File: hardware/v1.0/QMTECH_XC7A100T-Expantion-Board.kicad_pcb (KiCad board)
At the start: 4 copper layers, 99.1 x 98.5 mm, 132 parts, among them J1 Micro_SD_Card_Det1, J10 Conn_01x06, J11 Conn_01x04, J12 Conn_01x34, J13 Conn_02x10_Odd_Even, J14 USB_C_Receptacle_USB2.0_16P, J15 Conn_02x06_Top_Bottom, J16 Conn_02x06_Top_Bottom, J2 Conn_01x34, J3 USB_C_Receptacle_USB2.0_16P, J4 Conn_01x34, J5 Conn_01x03, J6 Conn_01x03, J7 Conn_01x04, J8 Conn_01x34, J9 Conn_01x34, Q1 AON6411, U10 74LVC245A, U11 TLV62585, U12 CH32V003JxMx, U13 TLV75718PDRV, U14 HUSB238, U15 CH340C, U2 CH32V003JxMx, U4 ADV7180BCP32Z-RL, U5 TLV62585, U6 74LVC245A, U7 TLV62585, U8 74LVC245A, U9 74LVC245A, Y1 28.63636MHz

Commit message: first schematic iteration done
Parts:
- added REF**: LED_0805_2012Metric, LED_SMD:LED_0805_2012Metric, F.Cu at (158.0, 103.4)
- added REF**: LED_0805_2012Metric, LED_SMD:LED_0805_2012Metric, F.Cu at (158.0, 105.4)
- added REF**: LED_0805_2012Metric, LED_SMD:LED_0805_2012Metric, F.Cu at (158.0, 107.4)
- added REF**: LED_0805_2012Metric, LED_SMD:LED_0805_2012Metric, F.Cu at (154.4, 103.4)
- added REF**: LED_0805_2012Metric, LED_SMD:LED_0805_2012Metric, F.Cu at (154.4, 107.5)
- added REF**: LED_0805_2012Metric, LED_SMD:LED_0805_2012Metric, F.Cu at (158.0, 101.3)
- added REF**: LED_0805_2012Metric, LED_SMD:LED_0805_2012Metric, F.Cu at (154.4, 105.4)
- added REF**: LED_0805_2012Metric, LED_SMD:LED_0805_2012Metric, F.Cu at (154.4, 101.3)
- added U16: ~, Package_DFN_QFN:Diodes_UDFN-10_1.0x2.5mm_P0.5mm, F.Cu at (39.5, 90.2)
- added U3: ~, Package_DFN_QFN:Diodes_UDFN-10_1.0x2.5mm_P0.5mm, F.Cu at (36.3, 90.2)
- J15, J16: value Conn_02x06_Top_Bottom -> Conn_02x06_Odd_Even
- moved J15 22.9 mm to (68.1, 92.9)
- moved J16 22.9 mm to (68.1, 70.0)
- moved U15 18.8 mm to (30.3, 94.0)
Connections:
- J14 pad A1: Net-(J14-GND-PadA1) -> GND
- J14 pad A12: Net-(J14-GND-PadA1) -> GND
- J14 pad A4: Net-(J14-VBUS-PadA4) -> unconnected-(J14-VBUS-PadA4)
- J14 pad A5: unconnected-(J14-CC1-PadA5) -> Net-(J14-CC1)
- J14 pad A6: unconnected-(J14-D+-PadA6) -> /UART_DP
- J14 pad A7: unconnected-(J14-D--PadA7) -> /UART_DN
- J14 pad A9: Net-(J14-VBUS-PadA4) -> unconnected-(J14-VBUS-PadA4)_2
- J14 pad B1: Net-(J14-GND-PadA1) -> GND
- J14 pad B12: Net-(J14-GND-PadA1) -> GND
- J14 pad B4: Net-(J14-VBUS-PadA4) -> unconnected-(J14-VBUS-PadA4)_1
- J14 pad B5: unconnected-(J14-CC2-PadB5) -> Net-(J14-CC2)
- J14 pad B6: unconnected-(J14-D+-PadB6) -> /UART_DP
- J14 pad B7: unconnected-(J14-D--PadB7) -> /UART_DN
- J14 pad B9: Net-(J14-VBUS-PadA4) -> unconnected-(J14-VBUS-PadA4)_3
- J14 pad S1: unconnected-(J14-SHIELD-PadS1) -> Net-(J14-SHIELD)
- J15 pad 1: unconnected-(J15-Pin_1-Pad1) -> /PMOD0_0P
- J15 pad 10: unconnected-(J15-Pin_10-Pad10) -> GND
- J15 pad 11: unconnected-(J15-Pin_11-Pad11) -> +3V3
- J15 pad 12: unconnected-(J15-Pin_12-Pad12) -> +3V3
- J15 pad 2: unconnected-(J15-Pin_2-Pad2) -> /PMOD0_0N
- J15 pad 3: unconnected-(J15-Pin_3-Pad3) -> /PMOD0_1P
- J15 pad 4: unconnected-(J15-Pin_4-Pad4) -> /PMOD0_1N
- J15 pad 5: unconnected-(J15-Pin_5-Pad5) -> /PMOD0_2P
- J15 pad 6: unconnected-(J15-Pin_6-Pad6) -> /PMOD0_2N
- J15 pad 7: unconnected-(J15-Pin_7-Pad7) -> /PMOD0_3P
- J15 pad 8: unconnected-(J15-Pin_8-Pad8) -> /PMOD0_3N
- J15 pad 9: unconnected-(J15-Pin_9-Pad9) -> GND
- J16 pad 1: unconnected-(J16-Pin_1-Pad1) -> /PMOD1_0P
- J16 pad 10: unconnected-(J16-Pin_10-Pad10) -> GND
- J16 pad 11: unconnected-(J16-Pin_11-Pad11) -> +3V3
- J16 pad 12: unconnected-(J16-Pin_12-Pad12) -> +3V3
- J16 pad 2: unconnected-(J16-Pin_2-Pad2) -> /PMOD1_0N
- J16 pad 3: unconnected-(J16-Pin_3-Pad3) -> /PMOD1_1P
- J16 pad 4: unconnected-(J16-Pin_4-Pad4) -> /PMOD1_1N
- J16 pad 5: unconnected-(J16-Pin_5-Pad5) -> /PMOD1_2P
- J16 pad 6: unconnected-(J16-Pin_6-Pad6) -> /PMOD1_2N
- J16 pad 7: unconnected-(J16-Pin_7-Pad7) -> /PMOD1_3P
- J16 pad 8: unconnected-(J16-Pin_8-Pad8) -> /PMOD1_3N
- J16 pad 9: unconnected-(J16-Pin_9-Pad9) -> GND
- J3 pad S1: GND -> Net-(J3-SHIELD)
- U1 pad 71: unconnected-(U1B-IO_B5-Pad71) -> /PMOD1_3P
- U1 pad 72: unconnected-(U1B-IO_A5-Pad72) -> /PMOD1_3N
- U1 pad 73: unconnected-(U1B-IO_B4-Pad73) -> /PMOD1_2P
- U1 pad 74: unconnected-(U1B-IO_A4-Pad74) -> /PMOD1_2N
- U1 pad 75: unconnected-(U1B-IO_A3-Pad75) -> /PMOD1_1P
- U1 pad 76: unconnected-(U1B-IO_A2-Pad76) -> /PMOD1_1N
- U1 pad 77: unconnected-(U1B-IO_D4-Pad77) -> /PMOD1_0P
- U1 pad 78: unconnected-(U1B-IO_C4-Pad78) -> /PMOD1_0N
- U1 pad 79: unconnected-(U1B-IO_C2-Pad79) -> /PMOD0_3P
- U1 pad 80: unconnected-(U1B-IO_B2_VREF-Pad80) -> /PMOD0_3N
- U1 pad 81: unconnected-(U1B-IO_E5-Pad81) -> /PMOD0_2P
- U1 pad 82: unconnected-(U1B-IO_D5-Pad82) -> /PMOD0_2N
- U1 pad 83: unconnected-(U1B-IO_C1-Pad83) -> /PMOD0_1P
- U1 pad 84: unconnected-(U1B-IO_B1-Pad84) -> /PMOD0_1N
- U1 pad 85: unconnected-(U1B-IO_E1-Pad85) -> /PMOD0_0P
- U1 pad 86: unconnected-(U1B-IO_D1-Pad86) -> /PMOD0_0N
- U15 pad 1: unconnected-(U15-GND-Pad1) -> GND
- U15 pad 16: unconnected-(U15-VCC-Pad16) -> +3V3
- U15 pad 2: unconnected-(U15-TXD-Pad2) -> /UART_TX
- U15 pad 3: unconnected-(U15-RXD-Pad3) -> /UART_RX
- U15 pad 4: unconnected-(U15-V3-Pad4) -> +3V3
- U15 pad 5: unconnected-(U15-UD+-Pad5) -> /UART_DP
- U15 pad 6: unconnected-(U15-UD--Pad6) -> /UART_DN
- U15 pad 7: unconnected-(U15-NC-Pad7) -> (no net)
- U15 pad 8: unconnected-(U15-NC-Pad8) -> (no net)
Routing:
- net unconnected-(J15-Pin_6-Pad6): track 46.9 -> 0.00 mm
- net unconnected-(J15-Pin_8-Pad8): track 46.5 -> 0.00 mm
- net unconnected-(J15-Pin_7-Pad7): track 45.9 -> 0.00 mm
- net unconnected-(J15-Pin_5-Pad5): track 45.7 -> 0.00 mm
- net unconnected-(J15-Pin_11-Pad11): track 42.7 -> 0.00 mm
- net unconnected-(J15-Pin_9-Pad9): track 41.6 -> 0.00 mm
- net unconnected-(J15-Pin_10-Pad10): track 39.7 -> 0.00 mm
- net unconnected-(J15-Pin_12-Pad12): track 39.5 -> 0.00 mm
- net unconnected-(J16-Pin_12-Pad12): track 22.5 -> 0.00 mm
- net unconnected-(J16-Pin_10-Pad10): track 22.5 -> 0.00 mm
- net unconnected-(J16-Pin_11-Pad11): track 21.2 -> 0.00 mm
- net unconnected-(J16-Pin_9-Pad9): track 20.9 -> 0.00 mm
- net unconnected-(J16-Pin_7-Pad7): track 18.7 -> 0.00 mm
- net unconnected-(J16-Pin_5-Pad5): track 17.4 -> 0.00 mm
- net unconnected-(J16-Pin_8-Pad8): track 16.8 -> 0.00 mm
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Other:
- board text added: "USART"
- board text added: "USB PD"

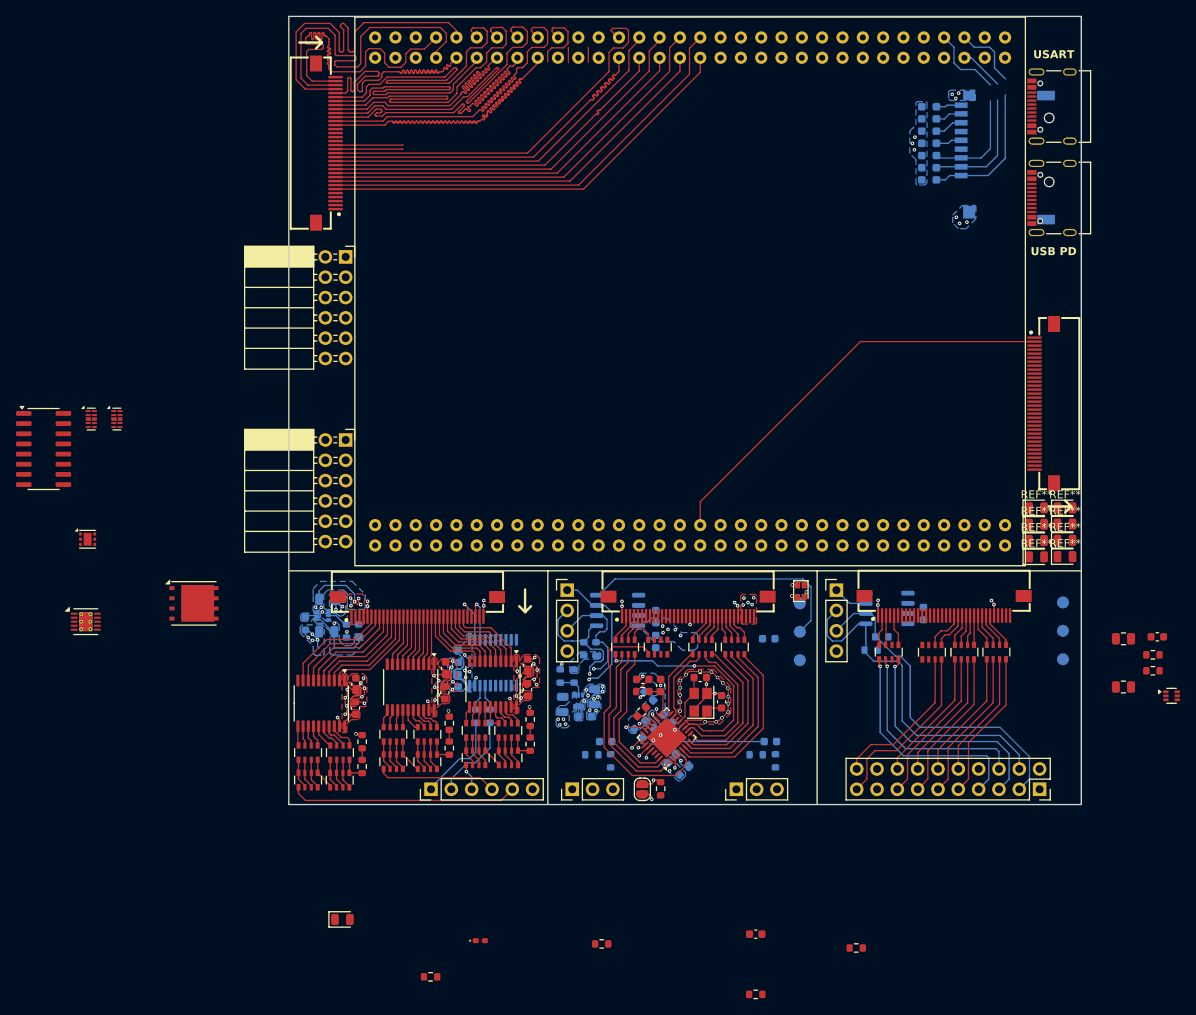
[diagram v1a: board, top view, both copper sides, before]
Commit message: did PORT0 routing
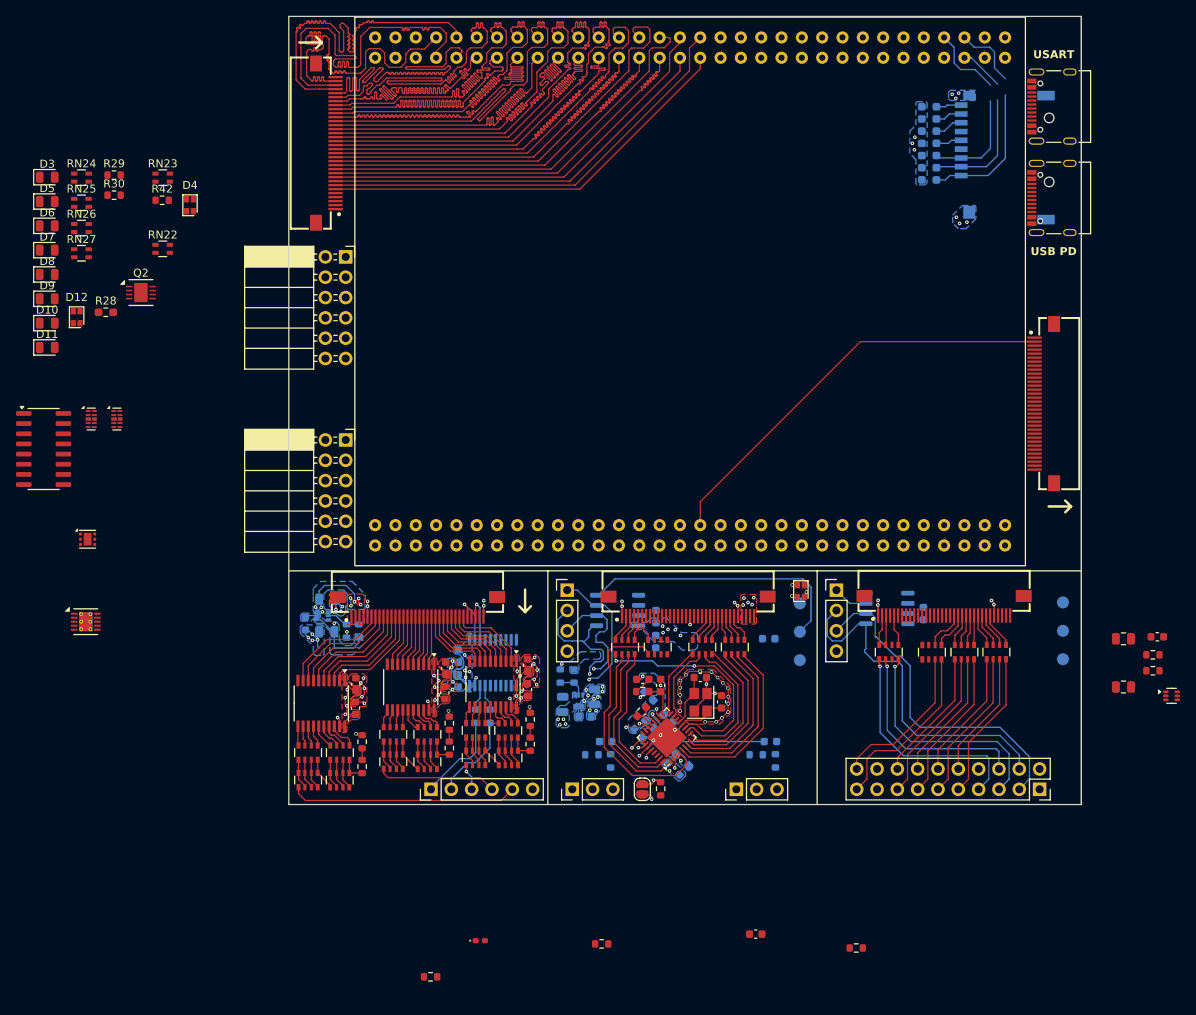
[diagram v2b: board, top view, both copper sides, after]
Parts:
- removed Q1: AON6411, Package_DFN_QFN:AO_DFN-8-1EP_5.55x5.2mm_P1.27mm_EP4.12x4.6mm
- removed R36, R37: 4.7k, Resistor_SMD:R_0603_1608Metric
- removed REF** (x8): LED_0805_2012Metric, LED_SMD:LED_0805_2012Metric
- added D10: ~, LED_SMD:LED_0805_2012Metric, F.Cu at (30.8, 78.3)
- added D11: ~, LED_SMD:LED_0805_2012Metric, F.Cu at (30.8, 81.3)
- added D12: ~, C779813:LED-SMD_4P-L1.6-W1.5-BR_TZ-P4-1615, F.Cu at (34.4, 77.5)
- added D4: ~, C779813:LED-SMD_4P-L1.6-W1.5-BR_TZ-P4-1615, F.Cu at (48.6, 63.5)
- added D5: ~, LED_SMD:LED_0805_2012Metric, F.Cu at (30.8, 63.1)
- added D6: ~, LED_SMD:LED_0805_2012Metric, F.Cu at (30.8, 66.1)
- added D7: ~, LED_SMD:LED_0805_2012Metric, F.Cu at (30.8, 69.1)
- added D8: ~, LED_SMD:LED_0805_2012Metric, F.Cu at (30.8, 72.2)
- added D9: ~, LED_SMD:LED_0805_2012Metric, F.Cu at (30.8, 75.2)
- added Q2: Q_PMOS_SGD, Package_DFN_QFN:DFN-8-1EP_3x3mm_P0.5mm_EP1.7x2.4mm, F.Cu at (42.5, 74.4)
- added R42: 5.1k, Resistor_SMD:R_0603_1608Metric, F.Cu at (45.1, 62.9)
- added RN22: 4.7k, Resistor_SMD:R_Array_Convex_2x0603, F.Cu at (45.2, 69.0)
- added RN23: 4.7k, Resistor_SMD:R_Array_Convex_2x0603, F.Cu at (45.2, 60.1)
- added RN24: 4.7k, Resistor_SMD:R_Array_Convex_2x0603, F.Cu at (35.0, 60.1)
- added RN25: 4.7k, Resistor_SMD:R_Array_Convex_2x0603, F.Cu at (35.0, 63.2)
- added RN26: 4.7k, Resistor_SMD:R_Array_Convex_2x0603, F.Cu at (35.0, 66.4)
- added RN27: 4.7k, Resistor_SMD:R_Array_Convex_2x0603, F.Cu at (35.0, 69.5)
- D2: value GREEN -> ~
- D3: value LED -> ~
- R13, R30: value 270 -> 5.1k
- R19: value 1k -> 5.1k
- R28: value 4.7k -> 5.1k; footprint Resistor_SMD:R_0603_1608Metric -> Resistor_SMD:R_0603_1608Metric_Pad0.98x0.95mm_HandSolder; moved to F.Cu
- R29: value 4.7k -> 5.1k; moved to F.Cu
- moved R30 128.1 mm to (39.1, 62.3)
- moved R29 112.0 mm to (39.1, 59.7), turned to 0 degrees
- moved R28 104.6 mm to (38.1, 76.9), turned to 0 degrees
- moved D3 99.8 mm to (30.8, 60.0)
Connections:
- D3 pad 1: GND -> Net-(D3-K)
- D3 pad 2: Net-(D3-A) -> /LED0_4
- J13 pad 1: +3V3 -> /OV7725-board/OV7725_P1
- J13 pad 10: /OV7725-board/OV7725_P8 -> /OV7725-board/OV7725_P6
- J13 pad 11: /OV7725-board/OV7725_P7 -> /OV7725-board/OV7725_P9
- J13 pad 12: /OV7725-board/OV7725_P6 -> /OV7725-board/OV7725_P8
- J13 pad 13: /OV7725-board/OV7725_P5 -> /OV7725-board/OV7725_CLK
- J13 pad 14: /OV7725-board/OV7725_P4 -> /OV7725-board/XCLK
- J13 pad 15: /OV7725-board/OV7725_P3 -> /OV7725-board/OV7725_VS
- J13 pad 16: /OV7725-board/OV7725_P2 -> /OV7725-board/OV7725_HS
- J13 pad 17: /OV7725-board/RST -> /OV7725-board/SCLK
- J13 pad 18: GND -> /OV7725-board/SDATA
- J13 pad 19: /OV7725-board/OV7725_P1 -> +3V3
- J13 pad 2: GND -> /OV7725-board/OV7725_P0
- J13 pad 20: /OV7725-board/OV7725_P0 -> GND
- J13 pad 3: /OV7725-board/SCLK -> /OV7725-board/RST
- J13 pad 4: /OV7725-board/SDATA -> GND
- J13 pad 5: /OV7725-board/OV7725_VS -> /OV7725-board/OV7725_P3
- J13 pad 6: /OV7725-board/OV7725_HS -> /OV7725-board/OV7725_P2
- J13 pad 7: /OV7725-board/OV7725_CLK -> /OV7725-board/OV7725_P5
- J13 pad 8: /OV7725-board/XCLK -> /OV7725-board/OV7725_P4
- J13 pad 9: /OV7725-board/OV7725_P9 -> /OV7725-board/OV7725_P7
- R28 pad 1: +3V3 -> Net-(D12-A)
- R28 pad 2: /OV7725-board/SDATA -> +3V3
- R29 pad 1: +3V3 -> GND
- R29 pad 2: /OV7725-board/SCLK -> Net-(J14-CC2)
- R30 pad 1: Net-(D3-A) -> GND
- R30 pad 2: +3V3 -> Net-(J14-CC1)
- U1 pad 95: unconnected-(U1B-IO_H2-Pad95) -> /STATUS1
- U1 pad 96: unconnected-(U1B-IO_H1-Pad96) -> /STATUS0
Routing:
- net /PORT0_GREEN3: track 0.00 -> 51.9 mm
- net /PORT0_GREEN1: track 0.00 -> 50.5 mm
- net /PORT0_GREEN2: track 1.88 -> 50.1 mm
- net /PORT0_GREEN5: track 8.41 -> 51.9 mm
- net /PORT0_GREEN0: track 9.31 -> 50.5 mm
- net /PORT0_GREEN4: track 10.3 -> 50.9 mm
- net /PORT0_BLUE3: track 34.7 -> 51.3 mm
- net /PORT0_VS: track 36.0 -> 51.8 mm
- net /PORT0_BLUE1: track 41.2 -> 50.4 mm
- net /PORT0_RED1: track 45.0 -> 52.1 mm
- net /PORT0_GREEN7: track 45.2 -> 51.9 mm
- net /PORT0_BLUE7: track 44.5 -> 50.8 mm
- net /PORT0_HS: track 45.7 -> 51.9 mm
- net /PORT0_BLUE6: track 44.8 -> 50.9 mm
- net /PORT0_RED0: track 46.0 -> 52.2 mm
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
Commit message: redoing 3v3 regulators
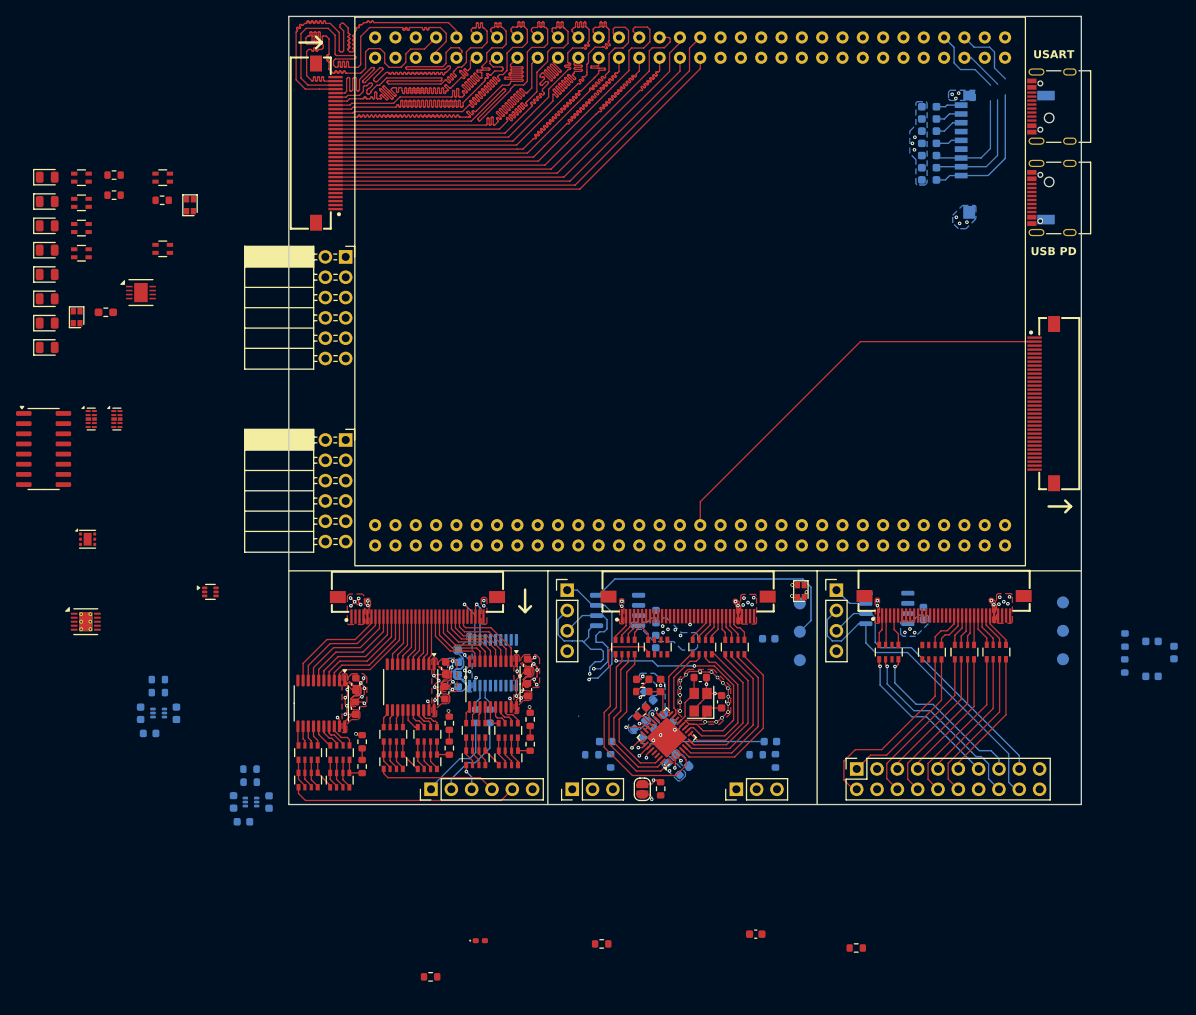
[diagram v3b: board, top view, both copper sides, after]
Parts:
- C10, C20, C27, C28: footprint Capacitor_SMD:C_0805_2012Metric -> Capacitor_SMD:C_0603_1608Metric
- C36, C39: footprint Capacitor_SMD:C_0805_2012Metric -> Capacitor_SMD:C_0603_1608Metric; moved to B.Cu
- L3, R31, R32: moved to B.Cu
- U11, U5, U7: value TLV62585 -> TLV62568DRL
- moved U11 120.9 mm to (51.2, 111.8)
- moved C20 47.0 mm to (54.1, 138.1)
- moved L1 44.7 mm to (55.3, 140.6), turned to 180 degrees
- moved U5 42.9 mm to (56.2, 138.1), turned to 180 degrees
- moved R15 42.2 mm to (56.1, 134.0), turned to 180 degrees
- moved R16 41.0 mm to (56.1, 135.6), turned to 0 degrees
- moved C10 38.7 mm to (58.5, 138.1)
- moved R21 26.2 mm to (44.7, 124.4), turned to 0 degrees
- moved C28 25.4 mm to (42.4, 127.0), turned to 90 degrees
- moved R20 24.3 mm to (44.7, 122.8), turned to 180 degrees
- moved U7 23.8 mm to (44.7, 127.0), turned to 180 degrees
- moved L2 23.8 mm to (43.6, 129.5), turned to 180 degrees
- moved C27 23.6 mm to (46.9, 127.0), turned to 90 degrees
- moved J13 23.0 mm to (132.0, 134.0), turned to 90 degrees
- moved C39 6.73 mm to (168.9, 118.0), turned to 180 degrees
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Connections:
- U11 pad 1: GND -> Net-(U11-FB)
- U11 pad 2: Net-(U11-SW) -> GND
- U11 pad 4: +5V -> Net-(U11-SW)
- U11 pad 5: Net-(U11-FB) -> +5V
- U5 pad 1: GND -> Net-(U5-FB)
- U5 pad 2: Net-(U5-SW) -> GND
- U5 pad 4: +5V -> Net-(U5-SW)
- U5 pad 5: Net-(U5-FB) -> +5V
- U7 pad 1: GND -> Net-(U7-FB)
- U7 pad 2: Net-(U7-SW) -> GND
- U7 pad 4: +5V -> Net-(U7-SW)
- U7 pad 5: Net-(U7-FB) -> +5V
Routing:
- net GND: track 96.8 -> 68.7 mm, vias 76 -> 66
- net +3V3: track 112.9 -> 99.4 mm, vias 36 -> 30
- net +5V: track 89.4 -> 78.0 mm, vias 17 -> 15
- net /OV7725-board/OV7725_CLK: track 28.5 -> 19.9 mm
- net /OV7725-board/OV7725_VS: track 29.3 -> 21.5 mm
- net /OV7725-board/SCLK: track 42.2 -> 34.6 mm
- net /OV7725-board/OV7725_P0: track 19.4 -> 23.8 mm
- net Net-(U7-FB): track 4.25 -> 0.00 mm
- net /OV7725-board/OV7725_P2: track 16.7 -> 20.3 mm
- net /OV7725-board/OV7725_P8: track 15.9 -> 19.4 mm
- net /OV7725-board/OV7725_P4: track 16.3 -> 19.9 mm
- net /OV7725-board/OV7725_P6: track 16.2 -> 19.8 mm
- net Net-(U5-FB): track 3.52 -> 0.00 mm
- net /OV7725-board/OV7725_P1: track 22.2 -> 19.3 mm
- net /OV7725-board/SDATA: track 43.7 -> 40.9 mm
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- removed copper zone on B.Cu, net +5V
- removed copper zone on B.Cu, net Net-(U5-SW)
- removed copper zone on B.Cu, net Net-(U7-SW)
